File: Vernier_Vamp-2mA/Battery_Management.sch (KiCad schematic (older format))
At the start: 49 parts, among them J4 Conn_02x07_Odd_Even, Q1 Si4447ADY, Q2 IRF8707PbF, SW1 DPDT_Hirose, U1 LM4040DBZ-5, U2 LM4040DBZ-5, U3 LM393

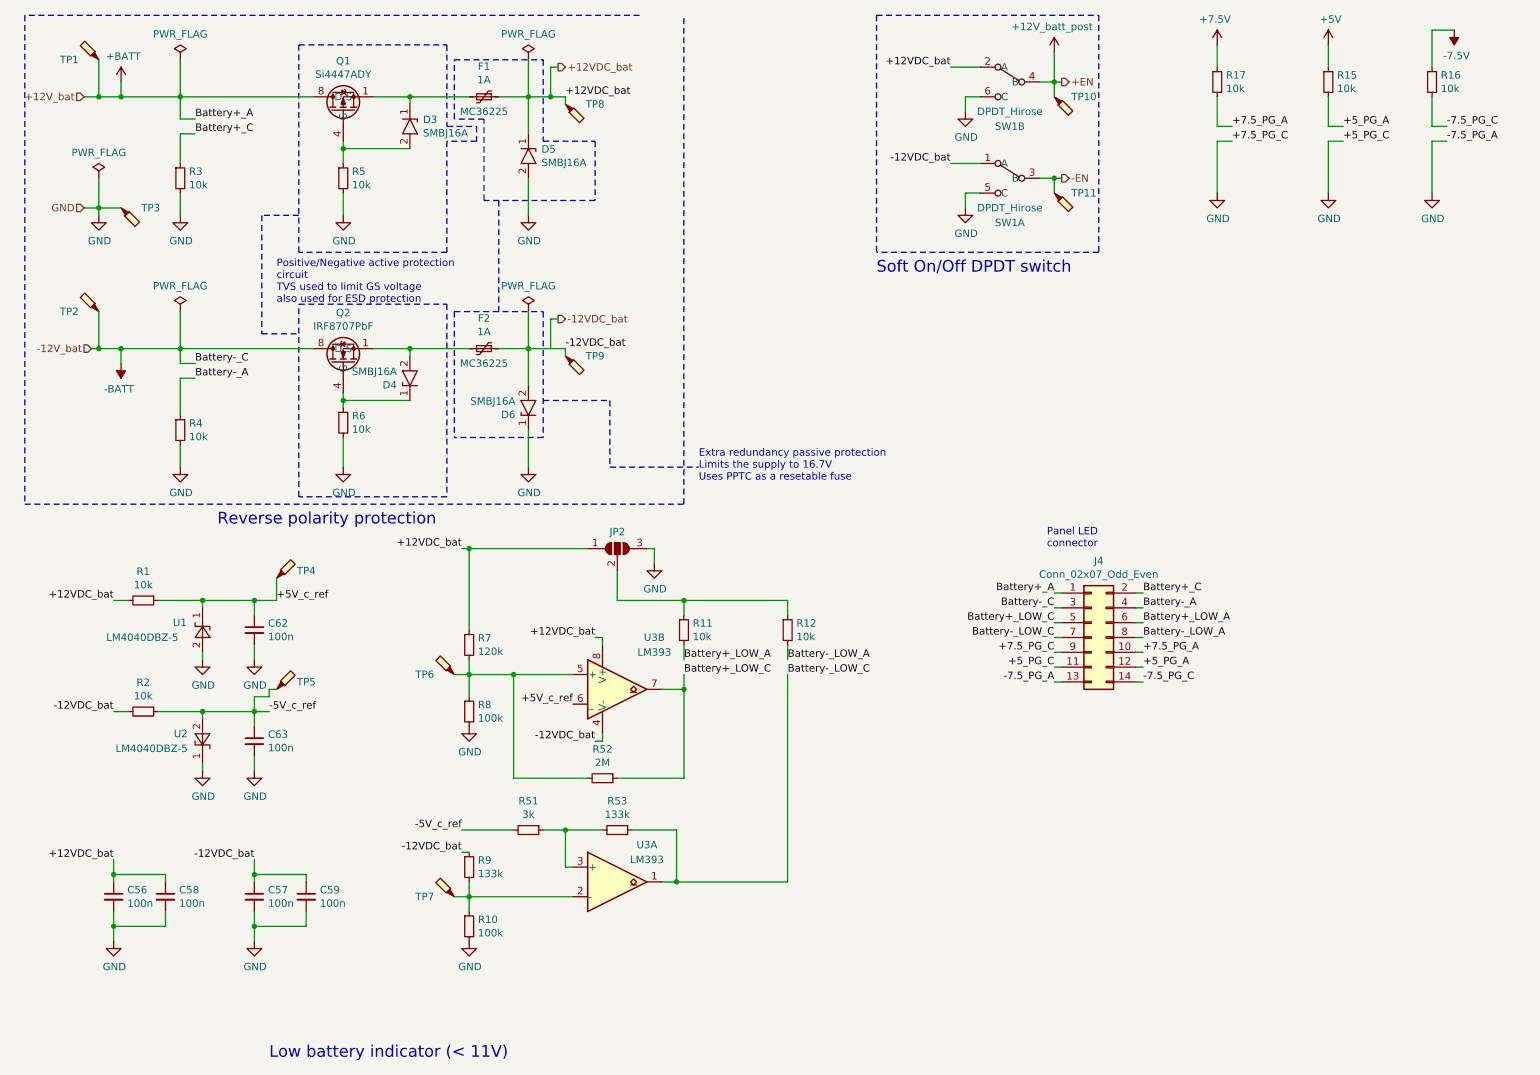
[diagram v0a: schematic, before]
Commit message: Applied 1.0B changes to 2mA version
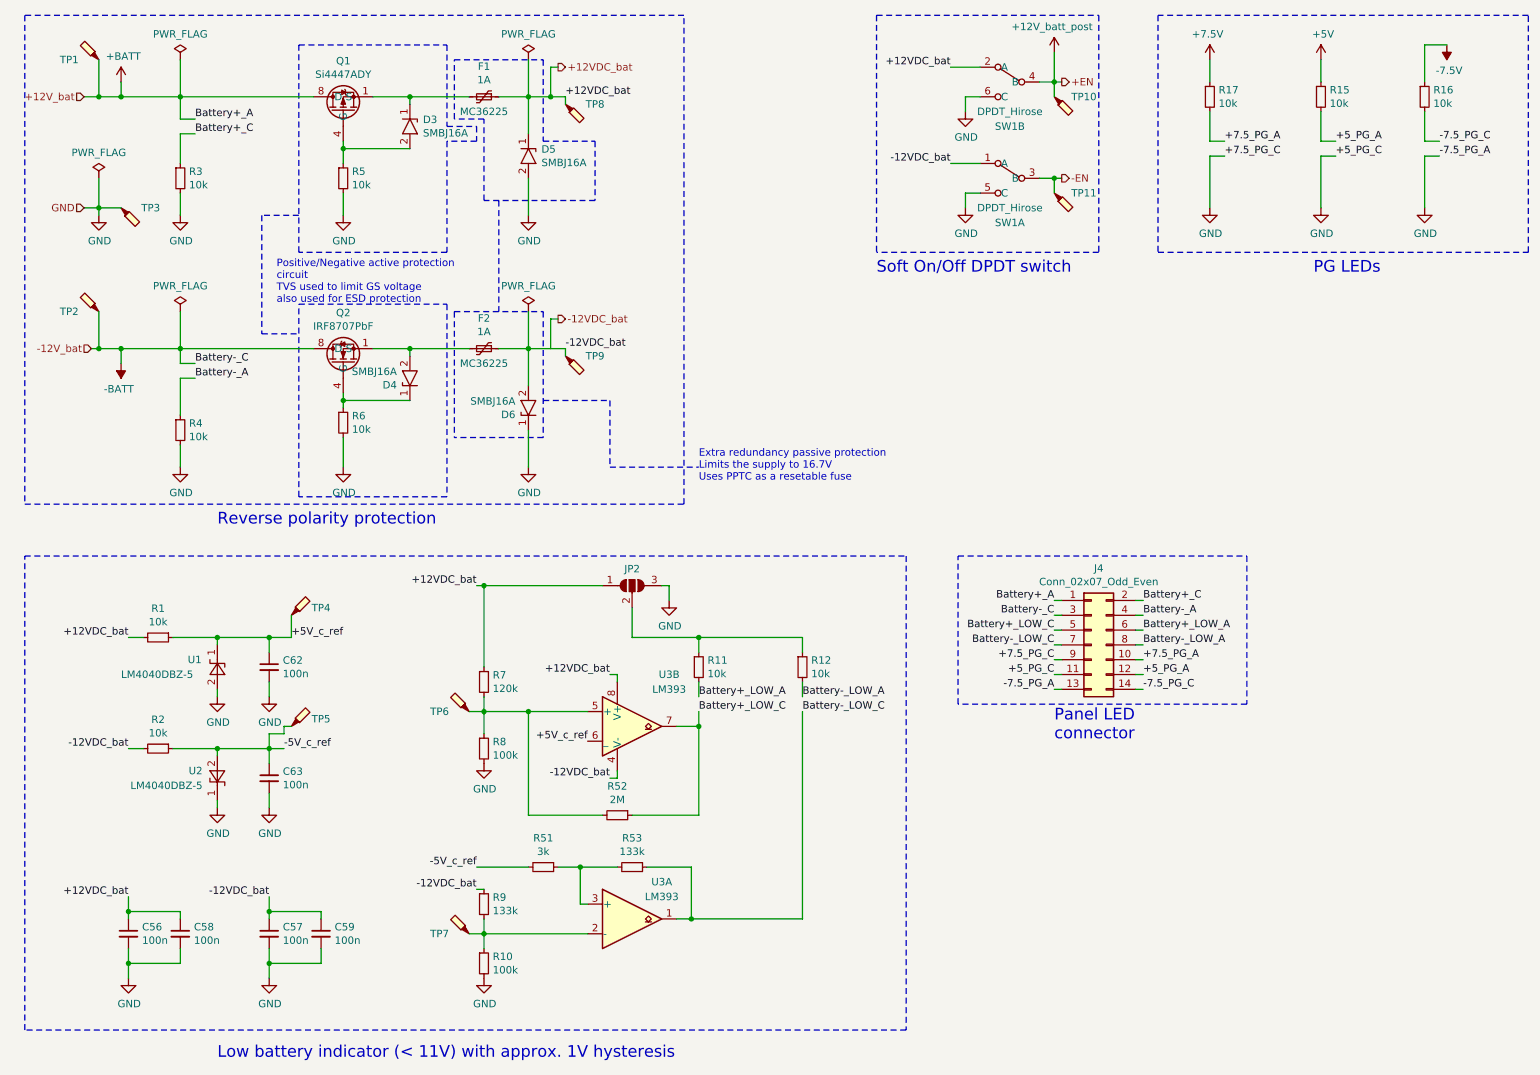
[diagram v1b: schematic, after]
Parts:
- SW1: footprint Connector_Harwin:Harwin_M20-7810245_2x02_P2.54mm_Vertical -> Connector_Hirose:Hirose_DF11-6DP-2DSA_2x03_P2.00mm_Vertical
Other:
- note added: "Low battery indicator (< 11V) with approx. 1V hysteresis\n"
- note added: "PG LEDs"
- note removed: "Low battery indicator (< 11V)\n"
- moved on the sheet: C56, C57, C58, C59, C62, C63, J4, JP2, R1, R10, R11, R12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

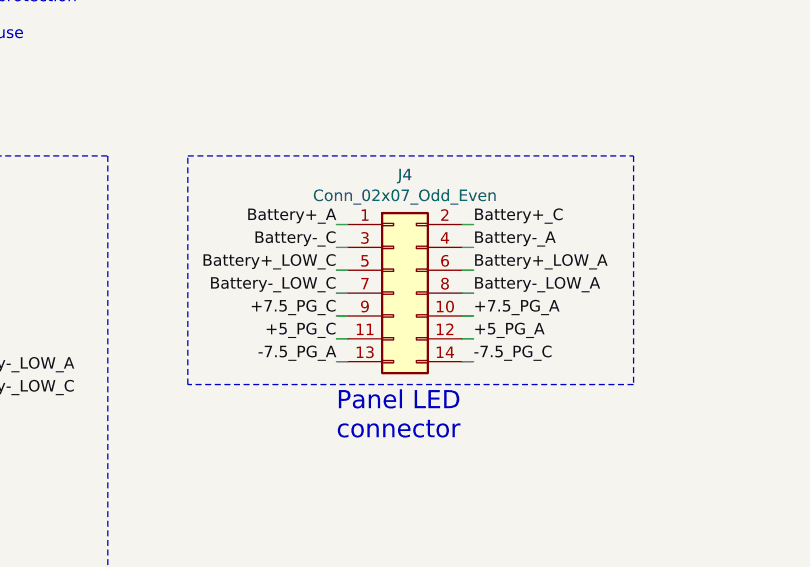
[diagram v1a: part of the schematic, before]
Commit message: 1.0C Initial commit
-Fixed amplifier output
-Changed connectors to IDC
-Via perimeter added
TODO:
Add shielding over analogue section
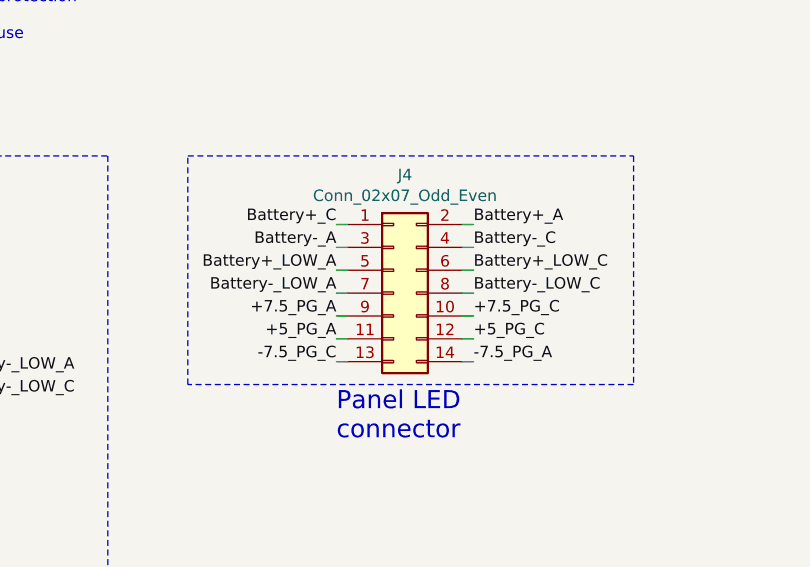
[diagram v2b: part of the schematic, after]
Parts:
- J4: footprint Connector_Hirose:Hirose_DF11-14DP-2DSA_2x07_P2.00mm_Vertical -> Connector_IDC:IDC-Header_2x07_P2.54mm_Vertical
- SW1: footprint Connector_Hirose:Hirose_DF11-6DP-2DSA_2x03_P2.00mm_Vertical -> Connector_IDC:IDC-Header_2x03_P2.54mm_Vertical
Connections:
- net +5_PG_A: now also J4.11 (Pin_11); no longer J4.12 (Pin_12)
- net +7.5_PG_A: now also J4.9 (Pin_9); no longer J4.10 (Pin_10)
- net +BATT: now also J4.2 (Pin_2); no longer J4.1 (Pin_1)
- net -7.5_PG_C: now also J4.13 (Pin_13); no longer J4.14 (Pin_14)
- net -BATT: now also J4.4 (Pin_4); no longer J4.3 (Pin_3)
- net Battery+_C: now also J4.1 (Pin_1); no longer J4.2 (Pin_2)
- net Battery+_LOW_A: now also J4.5 (Pin_5); no longer J4.6 (Pin_6)
- net Battery+_LOW_C: now also J4.6 (Pin_6); no longer J4.5 (Pin_5)
- net Battery-_A: now also J4.3 (Pin_3); no longer J4.4 (Pin_4)
- net Battery-_LOW_A: now also J4.7 (Pin_7); no longer J4.8 (Pin_8)
- net Battery-_LOW_C: now also J4.8 (Pin_8); no longer J4.7 (Pin_7)
- net GND: now also J4.10 (Pin_10), J4.12 (Pin_12), J4.14 (Pin_14); no longer J4.11 (Pin_11), J4.13 (Pin_13), J4.9 (Pin_9)
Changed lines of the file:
@@
 F 0 "SW1" H 7350 1050 50  0000 C CNN
 F 1 "DPDT_Hirose" H 7350 1150 50  0000 C CNN
-F 2 "Connector_Hirose:Hirose_DF11-6DP-2DSA_2x03_P2.00mm_Vertical" H 7350 1550 50  0001 C CNN
+F 2 "Connector_IDC:IDC-Header_2x03_P2.54mm_Vertical" H 7350 1550 50  0001 C CNN
 F 3 "" H 7350 1550 50  0001 C CNN
 	1    7350 1550
@@
 F 0 "SW1" H 7350 400 50  0000 C CNN
 F 1 "DPDT_Hirose" H 7350 500 50  0000 C CNN
-F 2 "Connector_Hirose:Hirose_DF11-6DP-2DSA_2x03_P2.00mm_Vertical" H 7350 900 50  0001 C CNN
+F 2 "Connector_IDC:IDC-Header_2x03_P2.54mm_Vertical" H 7350 900 50  0001 C CNN
 F 3 "" H 7350 900 50  0001 C CNN
 	2    7350 900
@@
 	1    0    0    -1
 $EndComp
-Text Label 7650 4600 2    50   ~ 0
+Text Label 8250 4600 0    50   ~ 0
 Battery+_A
-Text Label 7650 4700 2    50   ~ 0
+Text Label 8250 4700 0    50   ~ 0
 Battery-_C
-Text Label 7650 4800 2    50   ~ 0
+Text Label 8250 4800 0    50   ~ 0
 Battery+_LOW_C
-Text Label 7650 4900 2    50   ~ 0
+Text Label 8250 4900 0    50   ~ 0
 Battery-_LOW_C
-Text Label 7650 5000 2    50   ~ 0
+Text Label 8250 5000 0    50   ~ 0
 +7.5_PG_C
-Text Label 7650 5100 2    50   ~ 0
+Text Label 8250 5100 0    50   ~ 0
 +5_PG_C
 Text Label 8250 5200 0    50   ~ 0
--7.5_PG_C
-$Comp
-L Connector_Generic:Conn_02x07_Odd_Even J?
-U 1 1 5ECD6D57
-P 7900 4900
-AR Path="/5E1DD6A9/5ECD6D57" Ref="J?"  Part="1"
-AR Path="/5E1DD6A9/5EC279B2/5ECD6D57" Ref="J4"  Part="1"
-F 0 "J4" H 7950 5417 50  0000 C CNN
-F 1 "Conn_02x07_Odd_Even" H 7950 5326 50  0000 C CNN
-F 2 "Connector_Hirose:Hirose_DF11-14DP-2DSA_2x07_P2.00mm_Vertical" H 7900 4900 50  0001 C CNN
-F 3 "~" H 7900 4900 50  0001 C CNN
-	1    7900 4900
-	1    0    0    -1
-$EndComp
-Text Notes 7650 5550 0    79   ~ 0
-Panel LED\nconnector
-Text Label 8250 4600 0    50   ~ 0
-Battery+_C
-Text Label 8250 4700 0    50   ~ 0
-Battery-_A
-Text Label 8250 4800 0    50   ~ 0
-Battery+_LOW_A
-Text Label 8250 4900 0    50   ~ 0
-Battery-_LOW_A
-Text Label 8250 5000 0    50   ~ 0
-+7.5_PG_A
-Text Label 8250 5100 0    50   ~ 0
-+5_PG_A
-Text Label 7650 5200 2    50   ~ 0
 -7.5_PG_A
 Wire Wire Line
-	7700 4600 7650 4600
-Wire Wire Line
-	7700 4700 7650 4700
-Wire Wire Line
-	7700 4800 7650 4800
-Wire Wire Line
-	7700 4900 7650 4900
-Wire Wire Line
-	7700 5000 7650 5000
-Wire Wire Line
-	7700 5100 7650 5100
-Wire Wire Line
-	7700 5200 7650 5200
-Wire Wire Line
 	8200 4600 8250 4600
 Wire Wire Line
-	8250 4700 8200 4700
-Wire Wire Line
-	8250 4800 8200 4800
-Wire Wire Line
-	8250 4900 8200 4900
-Wire Wire Line
-	8250 5000 8200 5000
-Wire Wire Line
-	8250 5100 8200 5100
-Wire Wire Line
-	8250 5200 8200 5200
+	8200 4700 8250 4700
+Wire Wire Line
+	8200 4800 8250 4800
+Wire Wire Line
+	8200 4900 8250 4900
+Wire Wire Line
+	8200 5000 8250 5000
+Wire Wire Line
+	8200 5100 8250 5100
+Wire Wire Line
+	8200 5200 8250 5200
 $Comp
 L Device:R_Small R?
@@
 	8950 4300 8950 5300
 Wire Notes Line
-	8950 5300 7000 5300
-Wire Notes Line
 	7000 5300 7000 4300
 Wire Notes Line
@@
 Text Notes 9400 2400 0    79   ~ 0
 PG LEDs
+Wire Notes Line
+	8950 5300 7000 5300
+Text Notes 7650 5550 0    79   ~ 0
+Panel LED\nconnector
+$Comp
+L Connector_Generic:Conn_02x07_Odd_Even J?
+U 1 1 5ECD6D57
+P 7900 4900
+AR Path="/5E1DD6A9/5ECD6D57" Ref="J?"  Part="1"
+AR Path="/5E1DD6A9/5EC279B2/5ECD6D57" Ref="J4"  Part="1"
+F 0 "J4" H 7950 5417 50  0000 C CNN
+F 1 "Conn_02x07_Odd_Even" H 7950 5326 50  0000 C CNN
+F 2 "Connector_IDC:IDC-Header_2x07_P2.54mm_Vertical" H 7900 4900 50  0001 C CNN
+F 3 "~" H 7900 4900 50  0001 C CNN
+	1    7900 4900
+	1    0    0    -1
+$EndComp
+Wire Wire Line
+	7650 5200 7700 5200
+Wire Wire Line
+	7650 5100 7700 5100
+Wire Wire Line
+	7650 5000 7700 5000
+Wire Wire Line
+	7650 4900 7700 4900
+Wire Wire Line
+	7650 4800 7700 4800
+Wire Wire Line
+	7650 4700 7700 4700
+Wire Wire Line
+	7700 4600 7650 4600
+Text Label 7650 5100 2    50   ~ 0
++5_PG_A
+Text Label 7650 5000 2    50   ~ 0
++7.5_PG_A
+Text Label 7650 4900 2    50   ~ 0
+Battery-_LOW_A
+Text Label 7650 4800 2    50   ~ 0
+Battery+_LOW_A
+Text Label 7650 4700 2    50   ~ 0
+Battery-_A
+Text Label 7650 4600 2    50   ~ 0
+Battery+_C
+Text Label 7650 5200 2    50   ~ 0
+-7.5_PG_C
 $EndSCHEMATC
